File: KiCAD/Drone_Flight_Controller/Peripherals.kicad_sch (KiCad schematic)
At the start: 63 parts, among them J1 XT60, J2 0.5mΩ high side shunt, Q1 2N2222A, U1 74AHC1G125, U2 74AHC1G125, U3 74AHC1G125, U4 74AHC1G125, U9 INA195

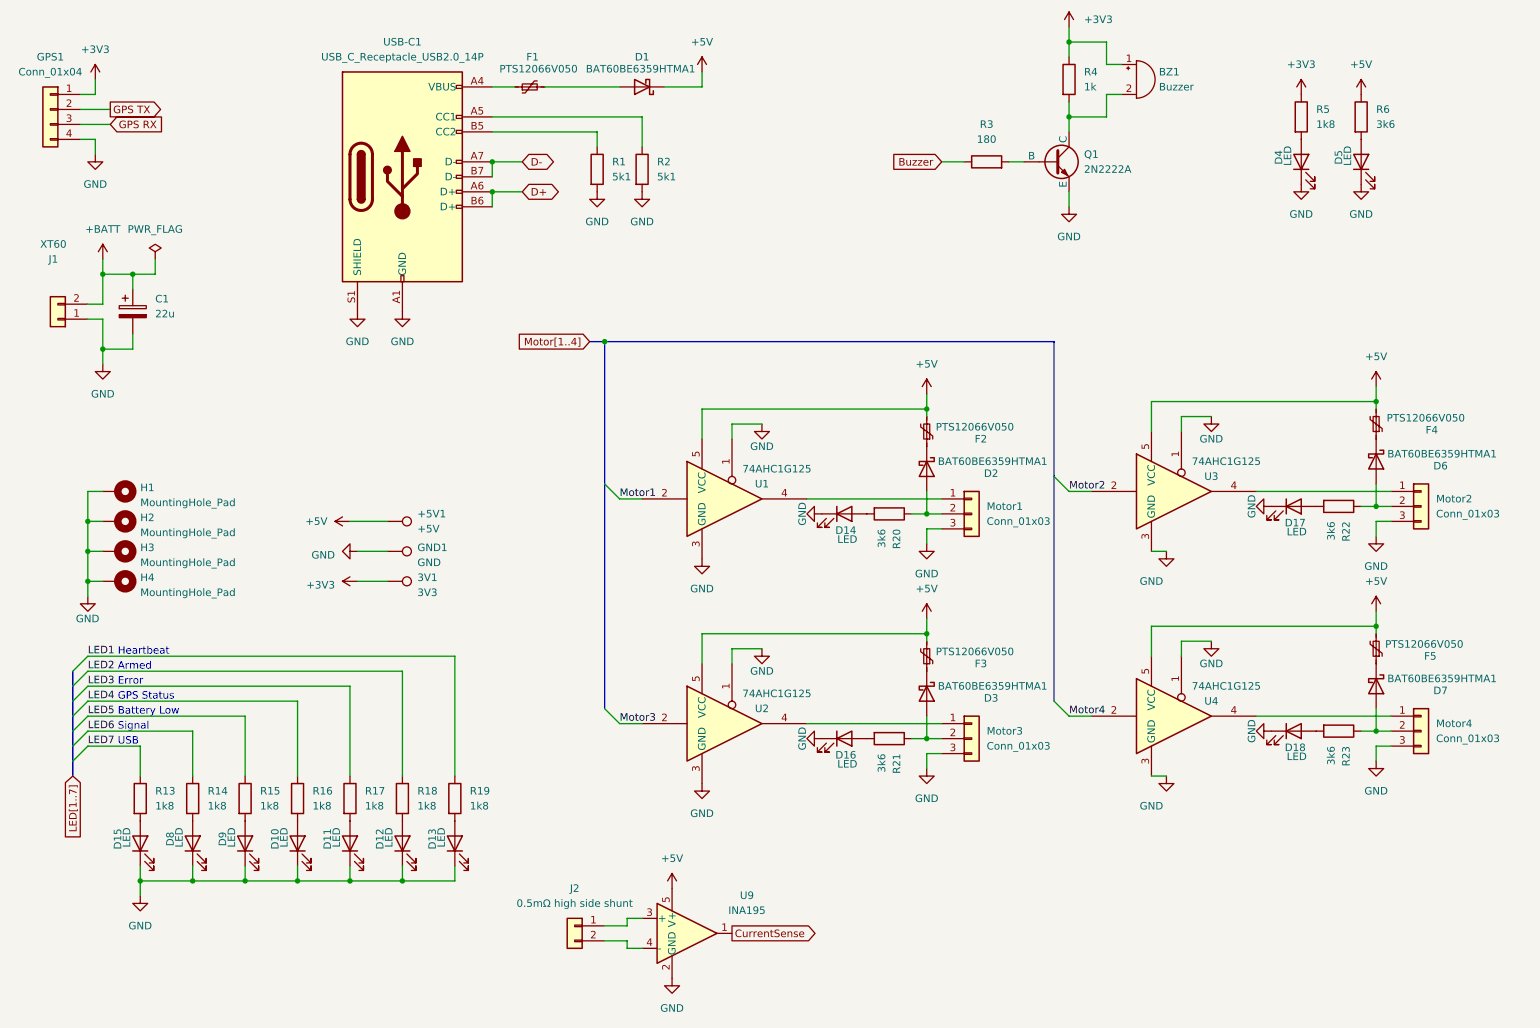
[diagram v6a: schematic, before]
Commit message: Implement feedback from Prof. Parzer
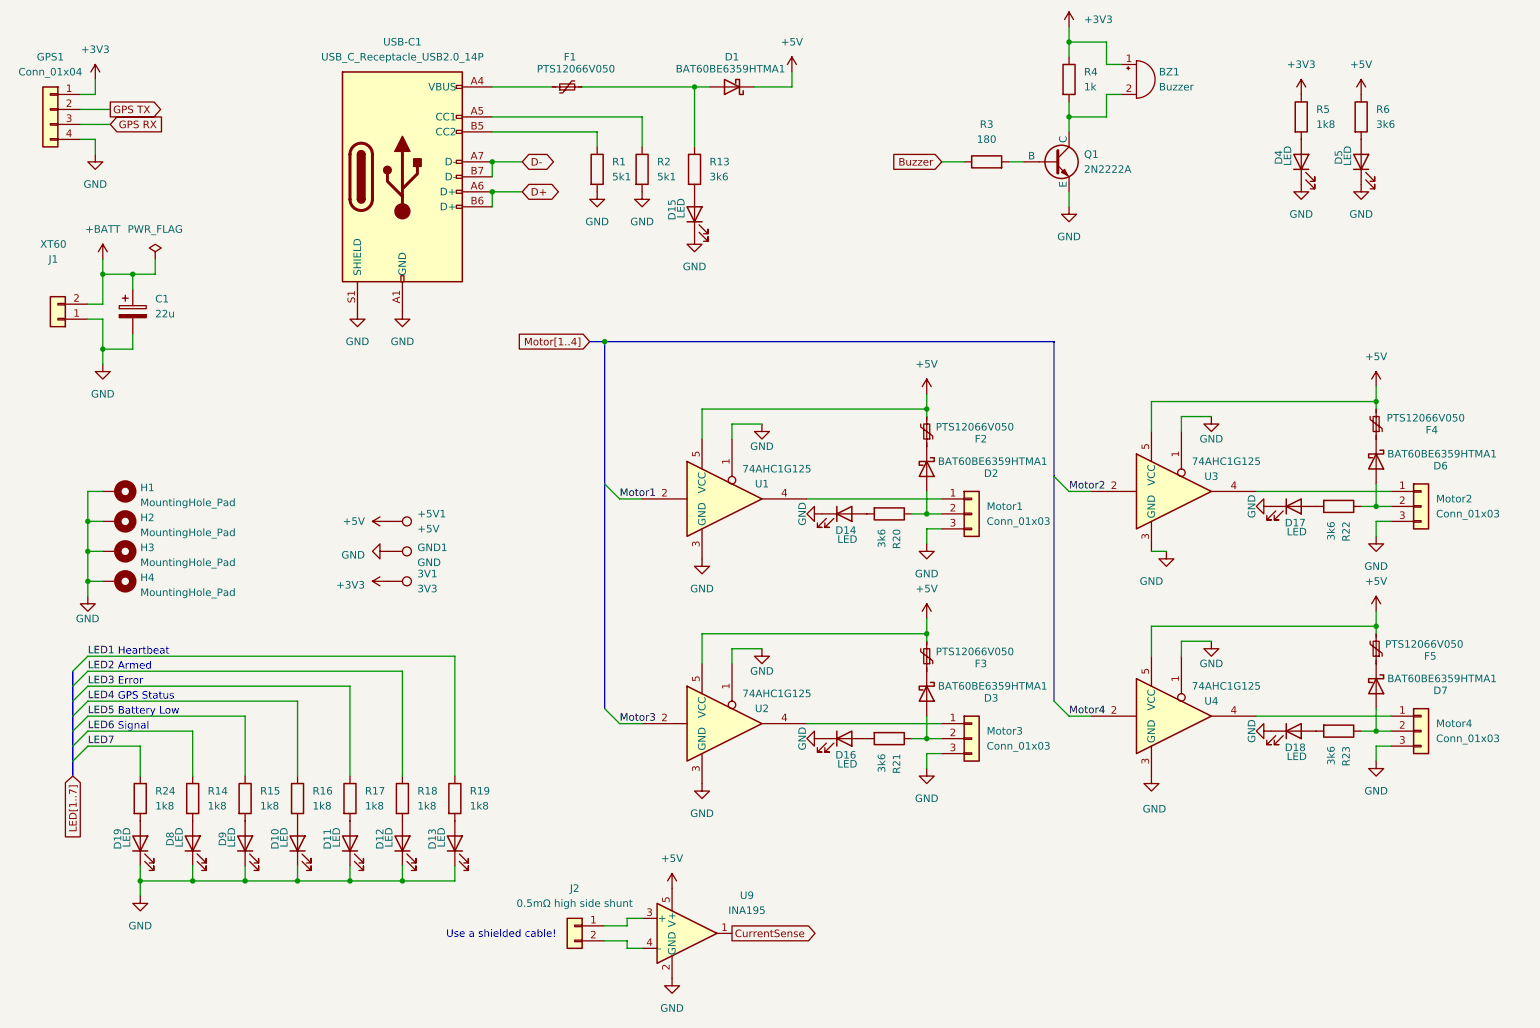
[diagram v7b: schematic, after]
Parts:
- added D19: LED, LED_SMD:LED_0805_2012Metric_Pad1.15x1.40mm_HandSolder, symbol Device:LED
- added R24: 1k8, Resistor_SMD:R_0805_2012Metric_Pad1.20x1.40mm_HandSolder, symbol Device:R
- GPS1: now in the parts list
- Motor1, Motor2, Motor3, Motor4: footprint Solder_Pad_3x_1x3mm:Solder_Pad_3x_1x3mm -> Connector_PinHeader_1.00mm:PinHeader_1x03_P1.00mm_Vertical; now in the parts list
- R13: value 1k8 -> 3k6
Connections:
- net GND: now also D19.1 (K)
- net LED7: now also R24.1; no longer R13.1
- net at D1.2 (A), F1.2: now also R13.1
- new net: D19.2 (A), R24.2
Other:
- note added: "Use a shielded cable!"
- note removed: "USB"
- moved on the sheet: D1, D15, F1, R13

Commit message: Fix wrong footprint
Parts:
- Motor1, Motor2, Motor3, Motor4: footprint Connector_PinHeader_1.00mm:PinHeader_1x03_P1.00mm_Vertical -> Connector_PinHeader_2.54mm:PinHeader_1x03_P2.54mm_Vertical
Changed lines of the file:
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@@
 			)
 		)
-		(property "Footprint" "Connector_PinHeader_1.00mm:PinHeader_1x03_P1.00mm_Vertical"
+		(property "Footprint" "Connector_PinHeader_2.54mm:PinHeader_1x03_P2.54mm_Vertical"
 			(at 264.16 147.32 0)
 			(effects
@@
 			)
 		)
-		(property "Footprint" "Connector_PinHeader_1.00mm:PinHeader_1x03_P1.00mm_Vertical"
+		(property "Footprint" "Connector_PinHeader_2.54mm:PinHeader_1x03_P2.54mm_Vertical"
 			(at 187.96 110.49 0)
 			(effects
@@
 			)
 		)
-		(property "Footprint" "Connector_PinHeader_1.00mm:PinHeader_1x03_P1.00mm_Vertical"
+		(property "Footprint" "Connector_PinHeader_2.54mm:PinHeader_1x03_P2.54mm_Vertical"
 			(at 264.16 109.22 0)
 			(effects
@@
 			)
 		)
-		(property "Footprint" "Connector_PinHeader_1.00mm:PinHeader_1x03_P1.00mm_Vertical"
+		(property "Footprint" "Connector_PinHeader_2.54mm:PinHeader_1x03_P2.54mm_Vertical"
 			(at 187.96 148.59 0)
 			(effects
